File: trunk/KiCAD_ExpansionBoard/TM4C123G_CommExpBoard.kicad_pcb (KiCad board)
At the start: 2 copper layers, 50.8 x 38.1 mm, 58 parts, among them J1 TI_BOOSTER_40_J1, J2 TI_BOOSTER_40_J2, J3 TI_BOOSTER_40_J3, J4 TI_BOOSTER_40_J4, P1 HEADER_2, P10 EB_GPIO0, P2 HEADER_2, P3 HEADER_2, P4 HEADER_2, P5 ANT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

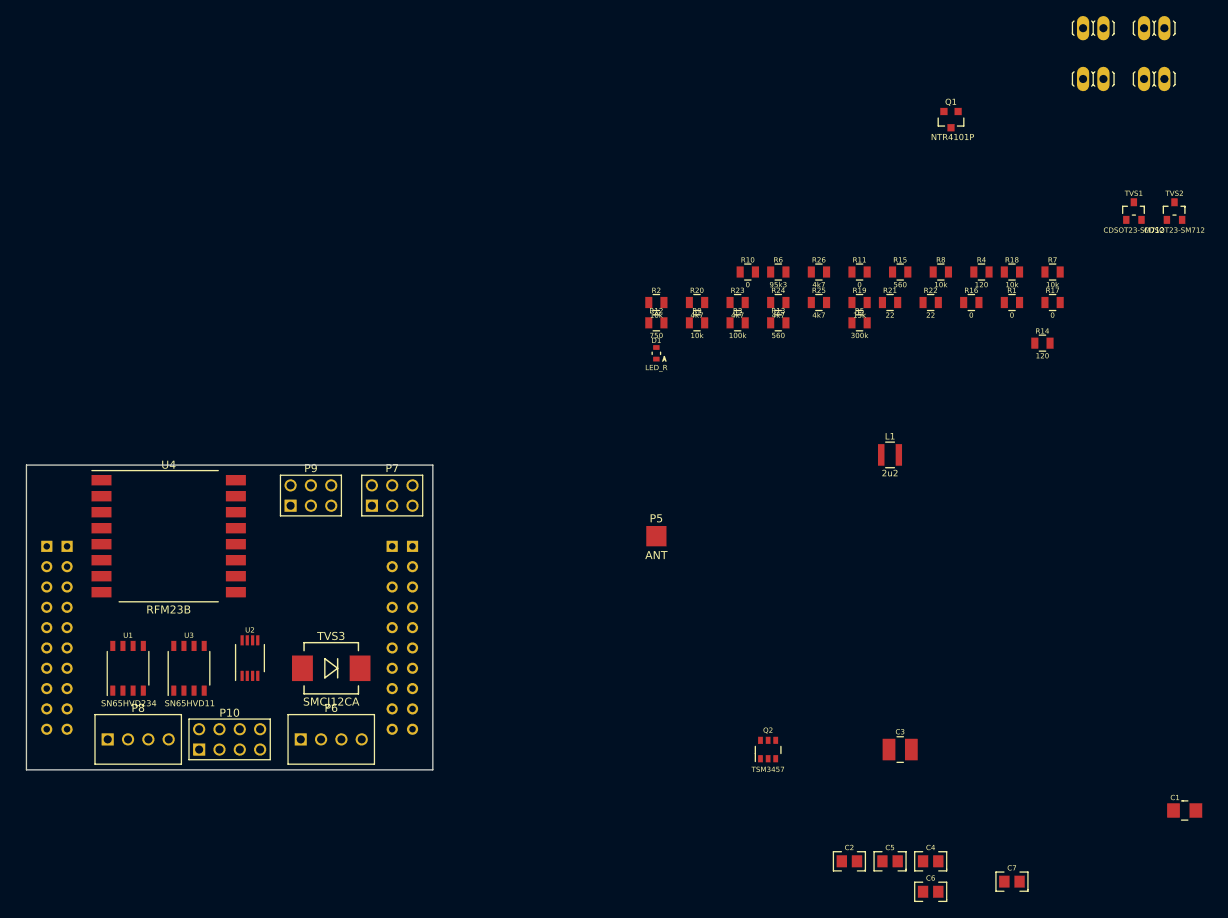
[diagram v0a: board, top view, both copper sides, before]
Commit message: -Unito le due linee a 3.3V e riposizionato Q1 che ora va ad interrompere la linea di alimentazione a 3.3V dello switching quando è presente la +5V_TLP (USB). In serie al gate ho messo R8 da 120 ohm e ho lasciato R7 da 10k di pull-down.
-Ho messo un NPN, Q3, che ha al suo interno un partitore da 22k + 47k; è pilotato dalla +5V_TLP ed ho messo R1 verso +12V_BUS che mantiene attivo lo switching a meno che non sia presente la +5V_TLP (Q3 ON). Infine ho posizionato il led a monte del PMOS.

-Per la protezione dalle sovratensioni sulla +5V_TLP ho inserito, all'ingesso, TVS4 che è bidirezionale con tensione di lavoro a 5V e tensione di breakdown di 5.8V (min).

-Rimosse tutte le resistenze di pull-up nei transceiver: ne avevano alcune già internamente.

-Sostituiti gli header-jumper per i terminatori e la rete di fail-safe biasing con un SPDT (SW1), ed un 4PDT (SW2).

In serie al pin RS del transceiver ho messo una 10k.

Pull-up da 10k su SDN dell'RF module
 
Ho inserito un secondo TP P1, ANT_GND che posizionerò vicino al primo, P5, ANT_C per il collegamento dell'antenna.

-MISURA DELLA TENSIONE DI BUS: V_AN_MONITOR: ho ricalcolato i valori di R19 e R20 per ottenere un divider ratio pari a 6.236 circa anziché 6.206 come indicato. La tensione di fondo scala sarà vicina ai 20 V.

-Il TVS3 (SMCJ12CA) indicato è bidirezionale (DS: http://www.farnell.com/datasheets/1794554.pdf), così ho corretto il simbolo mettendone uno appropriato.

-Sostituito lo "spare-function header" da 2x4 pin con uno 2x5 pin reimpostando pin-out come indicato, comprensivo di massa ed alimentazione.
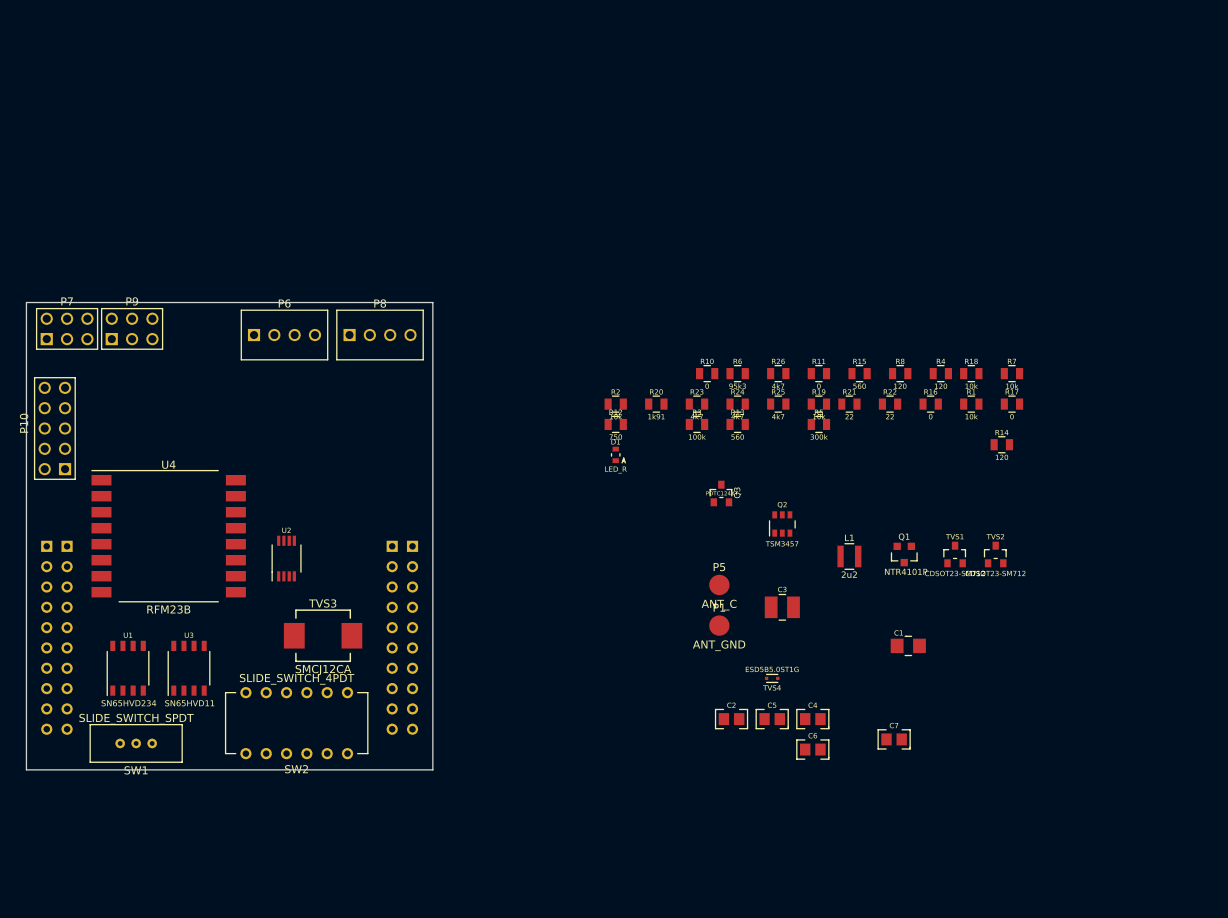
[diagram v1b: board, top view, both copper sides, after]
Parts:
- removed P2, P3, P4: HEADER_2, pinhead-1-1X02_MD
- removed R9: 10k, R_0805_MD
- added Q3: PDTC124XT, SOT23_MD, F.Cu at (212.6, 81.0)
- added SW1: SLIDE_SWITCH_SPDT, SPDT_SLIDE_SW_MD, F.Cu at (139.4, 112.3)
- added SW2: SLIDE_SWITCH_4PDT, 4PDT_SLIDE_SW_MD, F.Cu at (159.5, 109.7)
- added TVS4: ESD5B5.0ST1G, SOD-523_MD, F.Cu at (218.9, 104.1)
- P1: value HEADER_2 -> ANT_GND; footprint pinhead-1-1X02_MD -> ANT_PAD_MD
- P10: footprint pin_array_4x2_MD -> PIN_ARRAY_5x2_MD
- P5: value ANT -> ANT_C
- R1: value 0 -> 10k
- R19: value 15k -> 10k
- R20: value 4k7 -> 1k91
- R8: value 10k -> 120
- moved P1 88.1 mm to (212.3, 97.5)
- moved P8 58.9 mm to (169.9, 61.2)
- moved Q1 54.7 mm to (235.5, 88.6)
- moved P6 50.9 mm to (158.0, 61.2)
- moved TVS1 48.4 mm to (241.8, 88.6)
- moved TVS2 48.4 mm to (246.9, 88.6)
- moved P7 45.7 mm to (130.8, 60.5)
- moved P10 44.6 mm to (129.3, 72.9), turned to 90 degrees
- moved C1 40.2 mm to (236.0, 100.1)
- moved P9 30.6 mm to (138.9, 60.5)
- moved Q2 28.3 mm to (220.2, 84.8)
- moved C2 23.1 mm to (213.9, 109.2)
- moved C3 23.1 mm to (220.2, 95.2)
- moved C4 23.1 mm to (224.0, 109.2)
- moved C5 23.1 mm to (218.9, 109.2)
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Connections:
- C1 pad 1: N-0000067 (its old number) -> N-0000070
- C2 pad 1: N-0000073 -> +3.3V
- C3 pad 1: N-0000077 -> N-0000058
- C4 pad 1: N-0000059 (its old number) -> +3.3V
- D1 pad 1: N-0000077 -> N-0000057
- D1 pad 2: N-0000062 -> GND
- J1 pad 1: (no net) -> +3.3V
- J3 pad 1: (no net) -> +5V
- L1 pad 2: N-0000077 -> N-0000058
- P1 pad 1: N-0000071 -> GND
- P10 pad 1: /TM4C123G Connectors/EXT_AIN0 -> +3.3V
- P10 pad 2: /TM4C123G Connectors/EXT_AIN1 -> GND
- P10 pad 3: /TM4C123G Connectors/RFM_GPIO0 -> /TM4C123G Connectors/EXT_AIN0
- P10 pad 4: /Expansion Board/RFM_GPIO0 -> /TM4C123G Connectors/EXT_AIN1
- P10 pad 5: /TM4C123G Connectors/I2C0_SDA -> /TM4C123G Connectors/RFM_GPIO0
- P10 pad 6: /TM4C123G Connectors/I2C1_SDA -> /Expansion Board/RFM_GPIO0
- P10 pad 7: /TM4C123G Connectors/I2C0_SCL -> /TM4C123G Connectors/I2C0_SDA
- P10 pad 8: /TM4C123G Connectors/I2C1_SCL -> /TM4C123G Connectors/I2C0_SCL
- P7 pad 6: (no net) -> +3.3V
- P9 pad 6: (no net) -> +3.3V
- Q1 pad D: N-0000077 -> N-0000058
- Q1 pad G: N-0000061 -> N-0000072
- Q1 pad S: (no net) -> +3.3V
- R1 pad 1: N-0000060 -> N-0000070
- R1 pad 2: /Expansion Board/CAN0_RS -> N-0000073
- R10 pad 1: N-0000071 -> N-0000051
- R12 pad 1: GND -> N-0000057
- R12 pad 2: N-0000062 -> N-0000058
- R13 pad 1: N-0000063 -> +3.3V
- R13 pad 2: (no net) -> N-0000055
- R18 pad 1: (no net) -> +3.3V
- R18 pad 2: /Expansion Board/RFM_SSEL -> /Expansion Board/RFM_SDN
- R2 pad 1: /Expansion Board/CAN0_EN -> /Expansion Board/CAN0_RS
- R2 pad 2: GND -> N-0000056
- R23 pad 1: N-0000026 -> +3.3V
- R24 pad 1: N-0000026 -> +3.3V
- R25 pad 1: N-0000026 -> +3.3V
- R26 pad 1: N-0000026 -> +3.3V
- R3 pad 2: N-0000077 -> N-0000058
- R4 pad 2: N-0000069 -> N-0000075
- R5 pad 2: N-0000077 -> N-0000058
- R7 pad 1: N-0000061 -> N-0000064
- R8 pad 1: (no net) -> N-0000072
- R8 pad 2: /Expansion Board/RS485_RXEN# -> N-0000064
- TVS3 pad 1: GND -> /TM4C123G Connectors/+12V_BUS_UNP
- TVS3 pad 2: /TM4C123G Connectors/+12V_BUS_UNP -> GND
- U1 pad 3: N-0000073 -> +3.3V
- U1 pad 7: N-0000071 -> N-0000051
- U1 pad 8: N-0000060 -> N-0000056
- U2 pad 2: N-0000067 (its old number) -> N-0000070
- U2 pad 3: N-0000067 (its old number) -> N-0000073
- U2 pad 6: N-0000077 -> N-0000058
- U3 pad 8: N-0000059 (its old number) -> +3.3V
- U4 pad 5: (no net) -> +3.3V
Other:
- board size 50.8 x 38.1 mm -> 50.8 x 58.4 mm

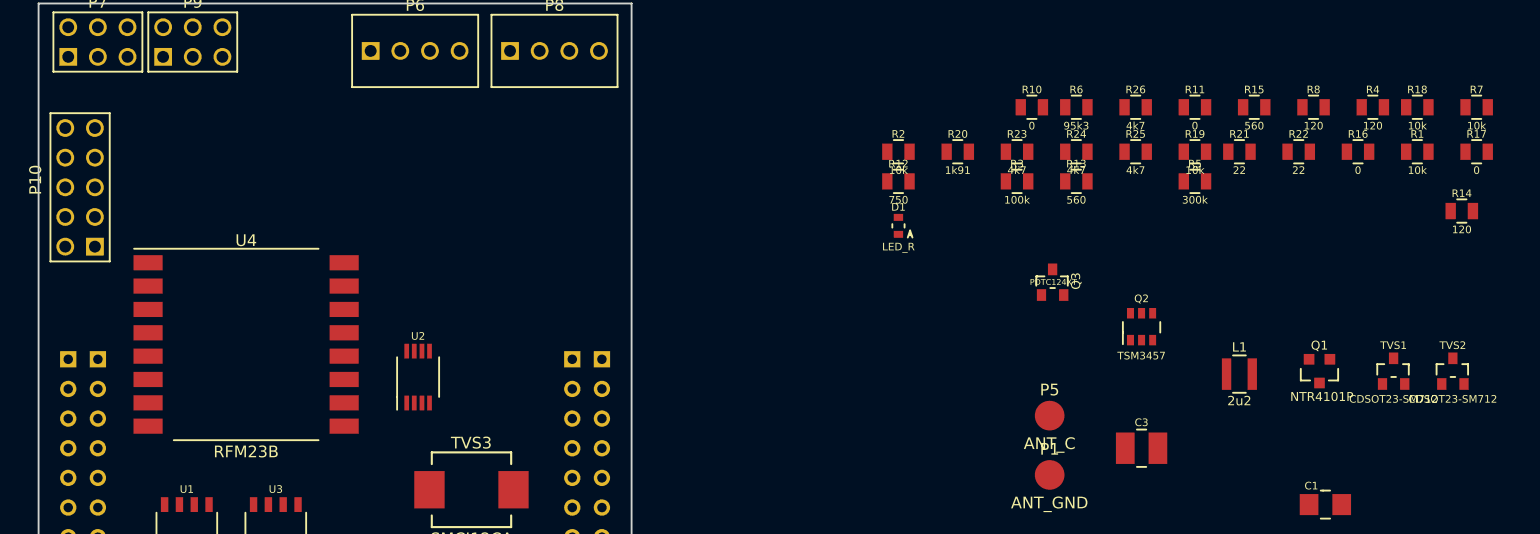
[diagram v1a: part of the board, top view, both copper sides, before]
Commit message: -Aggiunta R7 in serie a monte del TVS4. Se non occorre, sostituire con una 0ohm.
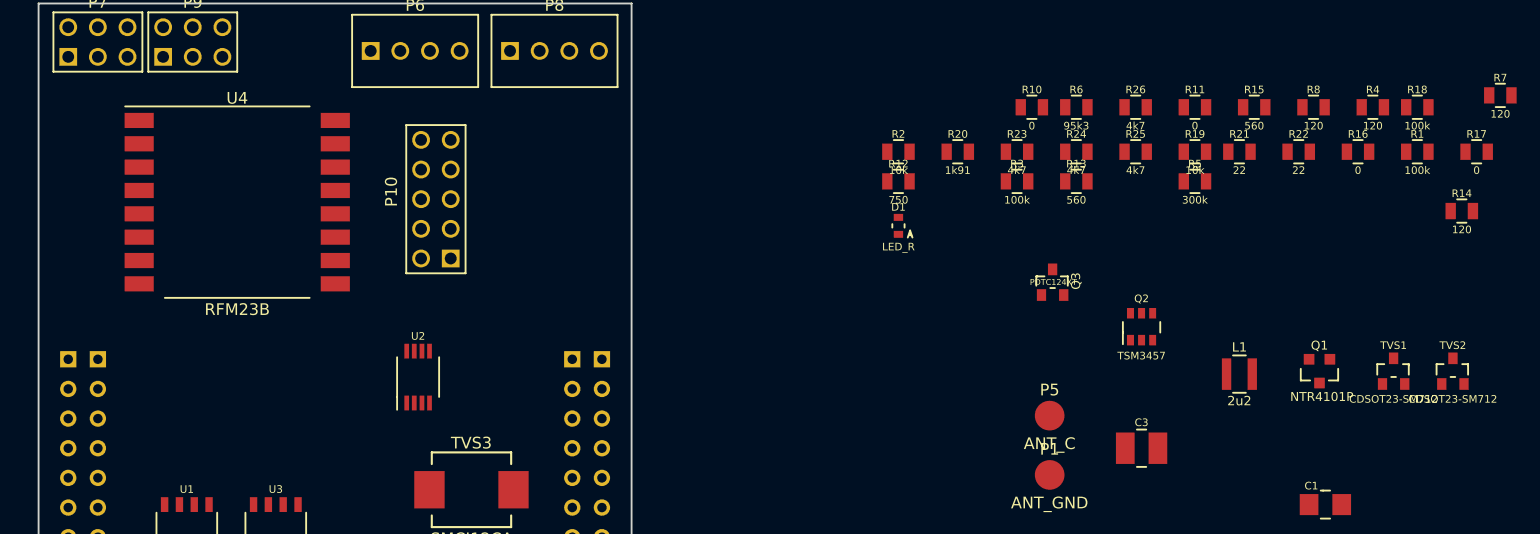
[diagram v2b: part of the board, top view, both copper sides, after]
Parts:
- R1, R18: value 10k -> 100k
- R7: value 10k -> 120
- moved P10 30.5 mm to (159.8, 73.9)
- moved U4 12.2 mm to (142.7, 74.2)
- moved R7 2.27 mm to (251.0, 65.0)
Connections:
- C1 pad 1: N-0000070 -> N-0000073
- J3 pad 1: +5V -> (no net)
- Q3 pad 3: N-0000073 -> N-0000075
- R1 pad 1: N-0000070 -> N-0000075
- R14 pad 1: N-0000066 (its old number) -> N-0000060
- R14 pad 2: N-0000068 -> N-0000077
- R15 pad 2: N-0000076 -> N-0000060
- R16 pad 1: N-0000067 (its old number) -> N-0000062
- R17 pad 1: N-0000066 (its old number) -> N-0000061
- R18 pad 1: +3.3V -> /Expansion Board/RFM_SDN
- R18 pad 2: /Expansion Board/RFM_SDN -> +3.3V
- R7 pad 1: N-0000064 (its old number) -> N-0000076
- R7 pad 2: GND -> (no net)
- R8 pad 2: N-0000064 (its old number) -> N-0000076
- SW2 pad 2: N-0000076 -> N-0000060
- SW2 pad 3: N-0000066 (its old number) -> N-0000061
- SW2 pad 5: N-0000068 -> N-0000077
- SW2 pad 6: N-0000067 (its old number) -> N-0000062
- SW2 pad 8: N-0000067 (its old number) -> N-0000077
- TVS4 pad 1: +5V -> GND
- TVS4 pad 2: GND -> N-0000076
- U2 pad 2: N-0000070 -> N-0000073
- U2 pad 3: N-0000073 -> N-0000075
- U3 pad 6: N-0000066 (its old number) -> N-0000061
- U3 pad 7: N-0000067 (its old number) -> N-0000062
